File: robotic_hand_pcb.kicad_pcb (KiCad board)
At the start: 4 copper layers, 55 x 73.5 mm, 125 parts, among them J1 2171750001, J10 A3, J11 A4, J12 A5, J13 A6, J14 A7, J15 JST 1x5 Male, J16 JST 1x5 Male, J17 JST 1x5 Male, J18 JST 1x5 Male, J19 JST 1x5 Male, J2 TC2050-IDC, J3 Battery, J4 Battery, J6 UART, J7 WS2812B, J8 A1, J9 A2, SW1 SPST, U1 LMR51430, U10 ACS712xLCTR-05B, U11 ACS712xLCTR-05B, U12 ACS712xLCTR-05B, U13 ACS712xLCTR-05B, U14 ULN2003ADR, U15 ULN2003ADR, U16 ULN2003ADR, U17 ULN2003ADR, U18 ULN2003ADR, U2 ld39150dt33-r, U3 TXB0104QPWRQ1, U4 STM32F446RET, U5 VL53L4CD, U7 BNO085, U8 ADS114S08, U9 ACS712xLCTR-05B, Y1 8M, Y2 32k768

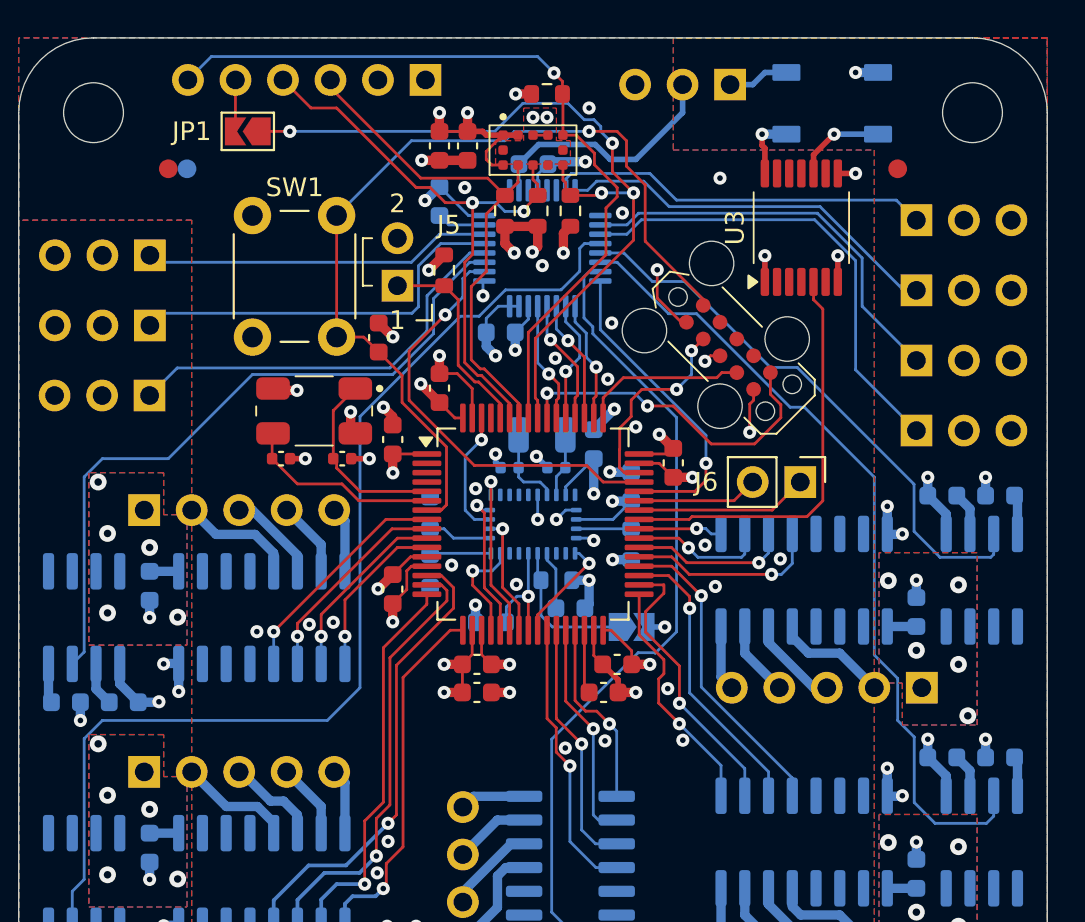
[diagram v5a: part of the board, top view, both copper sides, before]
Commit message: Fill empty spaces with GND pour
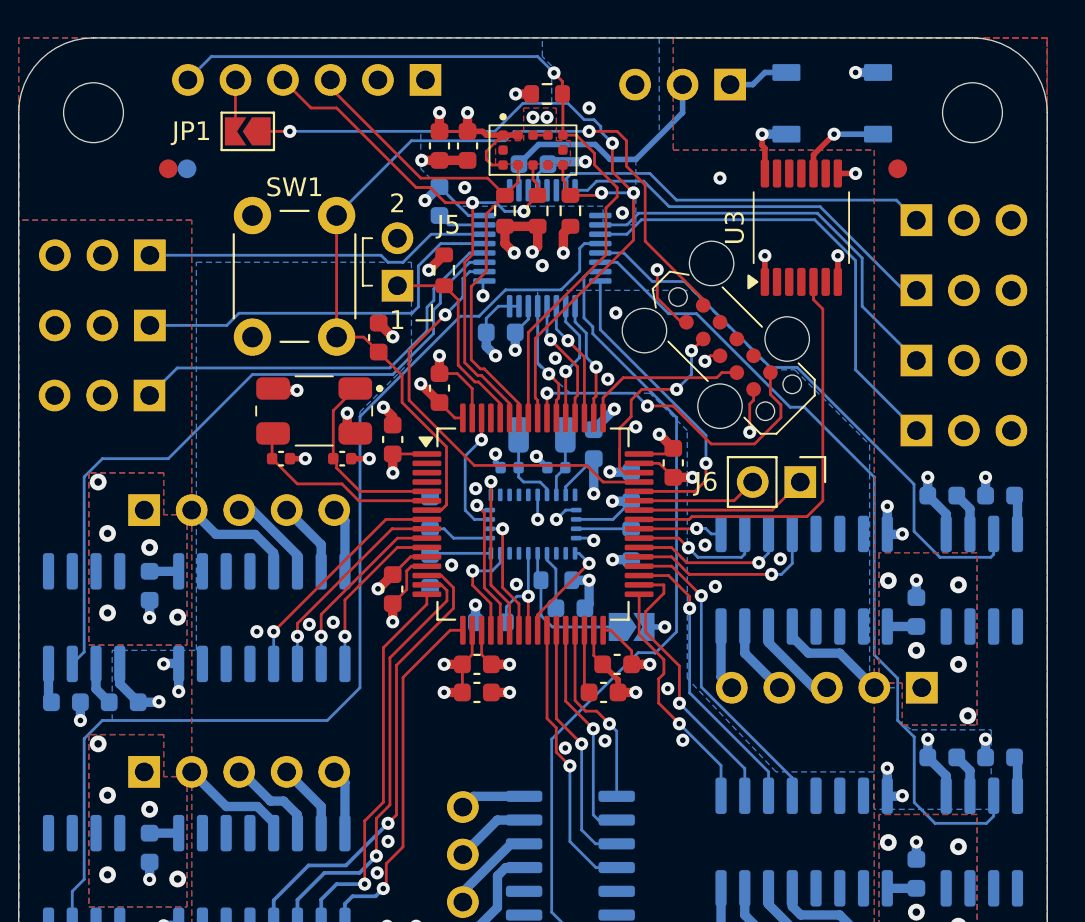
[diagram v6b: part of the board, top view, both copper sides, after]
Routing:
- added copper zone on B.Cu, net GND

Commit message: Add stitching vias and final touches
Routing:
- net GND: vias 98 -> 141
- net +5V: vias 7 -> 14
- net +3V3: vias 27 -> 28
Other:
- board text added: "J"
- board text added: "PWM"
- board text added: "TOF"
- board text added: "X"
- board text added: "Y"
- board text added: "Z"
- board text removed: "JU6"
